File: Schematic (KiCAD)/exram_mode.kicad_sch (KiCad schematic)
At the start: 86 parts

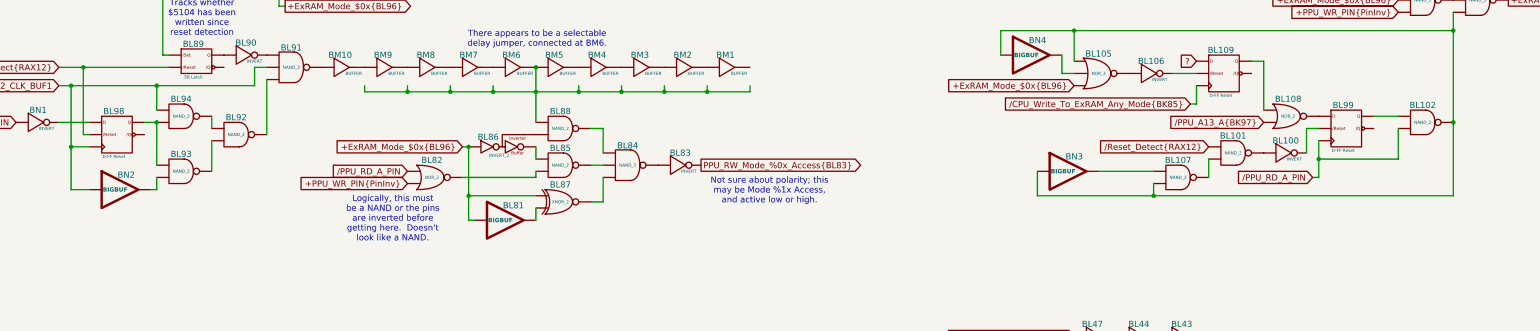
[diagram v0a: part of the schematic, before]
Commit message: - Started work on the pulse channels.  - Solved at least 2 of the red traces in the SVG.  - Finally realized that "Unknown 4to1" cells are actually just ordinary And-Or-Invert "AOI22" cells.
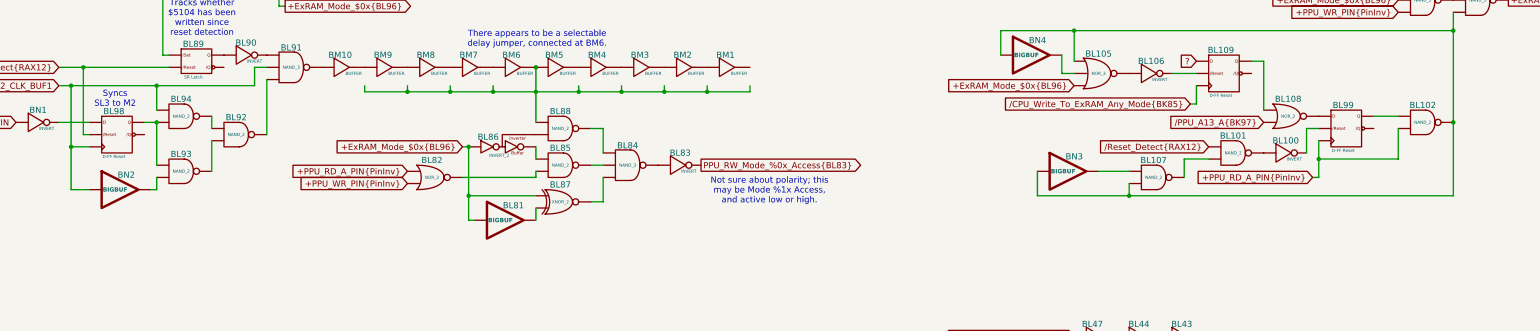
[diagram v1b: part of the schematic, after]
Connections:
- net at BL35. (X): now also BL34. (X), BL37. (X); no longer BL40. (X)
- net at BL31. (X): now also BL32. (X)
- net at BL32. (X): now also BL25. (X), BL28. (X); no longer BL31. (X)
- net at BL45. (X): now also BL41. (X); no longer BL46. (X)
- net at BL29. (X): now also BL35. (X); no longer BL30. (X)
- net +PPU_RD_A_PIN{PinInv}: now reaches BL99. (/Q)
- net +PPU_RD_A_PIN{PinInv}: now also BL102. (X), BL82. (X)
- net at BL100. (X): now also BL101. (X); no longer BL99. (/Q)
- net at BL39. (X): now also BL42. (X)
- net at BL90. (X): now also BL91. (X); no longer BL89. (/Q)
- net at BL44. (X): now also BL43. (X); no longer BL47. (X)
- net at BH9. (X): now also BK43. (X); no longer BH10. (X)
- net at BK43. (X): no longer BH9. (X)
- net at BL93. (X): now also BL92. (X); no longer BN2. (X)
- net at BL41. (X): now also BL42. (X); no longer BL45. (X)
- net at BL88. (X): now also BL86. (X); no longer BL84. (X)
- net at BL92. (X): now also BL94. (X); no longer BL93. (X)
- net at BM9. (X): now also BM10. (X); no longer BM8. (X)
- net at BM10. (X): now also BL91. (X); no longer BM9. (X)
- net at BH1. (X): now also BK41. (X); no longer BH2. (X)
- net at BK41. (X): no longer BH1. (X)
- net at BL84. (X): now also BL85. (X); no longer BL87. (X)
- net at BL85. (X): now also BL86. (X); no longer BL82. (X)
- net at BM3. (X): now also BM4. (X); no longer BM2. (X)
- net at BM4. (X): now also BM5. (X); no longer BM3. (X)
- net at BL106. (X): now also BL109. (/Q); no longer BL105. (X)
- net at BK40. (X): no longer BL9. (X)
- net at BK42. (X): no longer BL8. (X)
- removed net /PPU_RD_A_PIN: BL102. (X), BL82. (X), BL99. (/Q)
- new net: BL35. (X), BL40. (X)
- new net: BL45. (X), BL46. (X)
- new net: BL29. (X), BL32. (X), BL36. (X), BL41. (X), BL43. (X)
- new net: BL29. (X), BL32. (X), BL33. (X)
- new net: BL28. (X), BL29. (X), BL37. (X)
- new net: BL29. (X), BL30. (X)
- new net: BL81. (X), BL87. (X)
- new net: BK84. (X), BL102. (X), BL105. (X), BL107. (X), BN3. (X), BN4. (X)
- new net: BK83. (X), BK84. (X)
- new net: BK84. (X), BK86. (X)
- new net: BL102. (X), BL99. (/Q)
- new net: BL108. (X), BL99. (/Q)
- new net: BL100. (X), BL99. (/Q)
- new net: BL36. (X), BL37. (X)
- new net: BL93. (X), BL94. (X), BL98. (/Q)
- new net: BL98. (/Q), BN1. (X)
- new net: BK79. (X), BK81. (X), BK82. (Q1)
- new net: BL89. (/Q), BL90. (X)
- new net: BL44. (X), BL47. (X)
- new net: BH10. (X), BH9. (X)
- new net: BL93. (X), BN2. (X)
- new net: BK39. (X), BK40. (X), BK42. (X)
- new net: BL37. (X), BL38. (X), BL42. (X)
- new net: BL84. (X), BL88. (X)
- new net: BL88. (X), BM5. (X), BM6. (X)
- new net: BM8. (X), BM9. (X)
- new net: BL108. (X), BL109. (/Q)
- new net: BK79. (X), BK82. (Q1), BL96. (X)
- new net: BH1. (X), BH2. (X)
- new net: BL84. (X), BL87. (X)
- new net: BL82. (X), BL85. (X)
- new net: BL83. (X), BL84. (X)
- new net: BK41. (X), BK43. (X), BK44. (X)
- new net: BM2. (X), BM3. (X)
- new net: BK80. (X), BK82. (Q1)
- new net: BL105. (X), BL106. (X)
- new net: BL91. (X), BL92. (X)
- new net: BK40. (X), BL9. (X)
- new net: BK42. (X), BL8. (X)
- now unconnected: BK40. (X), BK41. (X), BK42. (X), BK43. (X)
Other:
- note added: "Syncs SL3 to M2"
- note removed: "Logically, this must be a NAND or the pins are inverted before getting here. Doesn't look like a NAND."
- moved on the sheet: BL107
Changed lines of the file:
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@@
 		)
 	)
-	(text "There appears to be a selectable\ndelay jumper, connected at BM6."
+	(text "Syncs\nSL3 to M2"
 		(exclude_from_sim no)
-		(at 151.384 103.378 0)
+		(at 63.754 115.824 0)
 		(effects
 			(font
@@
 		)
 	)
-	(text "Logically, this must\nbe a NAND or the pins\nare inverted before\ngetting here.  Doesn't\nlook like a NAND."
+	(text "There appears to be a selectable\ndelay jumper, connected at BM6."
 		(exclude_from_sim no)
-		(at 121.412 140.716 0)
+		(at 151.384 103.378 0)
 		(effects
 			(font
@@
 	)
 	(junction
+		(at 274.32 135.89)
+		(diameter 0)
+		(color 0 0 0 0)
+	)
+	(junction
 		(at 290.83 204.47)
 		(diameter 0)
@@
 	)
 	(junction
-		(at 279.4 135.89)
-		(diameter 0)
-		(color 0 0 0 0)
-	)
-	(junction
 		(at 54.61 113.03)
 		(diameter 0)
@@
 	(wire
 		(pts
-			(xy 267.97 130.81) (xy 279.4 130.81)
+			(xy 267.97 130.81) (xy 274.32 130.81)
 		)
 		(stroke
@@
 	(wire
 		(pts
-			(xy 341.63 135.89) (xy 279.4 135.89)
-		)
-		(stroke
-			(width 0)
-			(type default)
-		)
-	)
-	(wire
-		(pts
 			(xy 177.8 113.03) (xy 177.8 114.3)
 		)
@@
 	(wire
 		(pts
-			(xy 290.83 128.27) (xy 290.83 132.08)
+			(xy 285.75 128.27) (xy 285.75 132.08)
 		)
 		(stroke
@@
 	(wire
 		(pts
+			(xy 274.32 135.89) (xy 255.27 135.89)
+		)
+		(stroke
+			(width 0)
+			(type default)
+		)
+	)
+	(wire
+		(pts
 			(xy 52.07 113.03) (xy 54.61 113.03)
 		)
@@
 	(wire
 		(pts
-			(xy 279.4 135.89) (xy 279.4 133.35)
+			(xy 274.32 135.89) (xy 274.32 133.35)
 		)
 		(stroke
@@
 	(wire
 		(pts
+			(xy 285.75 128.27) (xy 290.83 128.27)
+		)
+		(stroke
+			(width 0)
+			(type default)
+		)
+	)
+	(wire
+		(pts
+			(xy 274.32 135.89) (xy 341.63 135.89)
+		)
+		(stroke
+			(width 0)
+			(type default)
+		)
+	)
+	(wire
+		(pts
 			(xy 328.93 165.1) (xy 290.83 165.1)
 		)
@@
 	(wire
 		(pts
-			(xy 279.4 135.89) (xy 255.27 135.89)
-		)
-		(stroke
-			(width 0)
-			(type default)
-		)
-	)
-	(wire
-		(pts
 			(xy 323.85 74.93) (xy 327.66 74.93)
 		)
@@
 		)
 	)
-	(global_label "{slash}PPU_RD_A_PIN"
+	(global_label "+PPU_RD_A_PIN{PinInv}"
 		(shape input)
 		(at 124.46 130.81 180)
@@
 		)
 		(property "Intersheetrefs" "${INTERSHEET_REFS}"
-			(at 106.5371 130.81 0)
+			(at 98.8566 130.81 0)
 			(effects
 				(font
@@
 		)
 	)
-	(global_label "{slash}PPU_RD_A_PIN"
+	(global_label "+PPU_RD_A_PIN{PinInv}"
 		(shape input)
 		(at 312.42 132.08 180)
@@
 		)
 		(property "Intersheetrefs" "${INTERSHEET_REFS}"
-			(at 294.4971 132.08 0)
+			(at 286.8166 132.08 0)
 			(effects
 				(font
@@
 		(lib_name "NAND_2_11")
 		(lib_id "MMC5:NAND_2")
-		(at 284.48 132.08 0)
+		(at 279.4 132.08 0)
 		(unit 1)
 		(exclude_from_sim no)
@@
 		(fields_autoplaced yes)
 		(property "Reference" "BL107"
-			(at 284.48 127.762 0)
+			(at 279.4 127.762 0)
 			(do_not_autoplace yes)
 			(effects
@@
 		)
 		(property "Value" "NAND_2"
-			(at 284.48 132.08 0)
+			(at 279.4 132.08 0)
 			(do_not_autoplace yes)
 			(effects
@@
 		)
 		(property "Footprint" ""
-			(at 284.48 132.08 0)
+			(at 279.4 132.08 0)
 			(effects
 				(font
@@
 		)
 		(property "Datasheet" ""
-			(at 284.48 132.08 0)
+			(at 279.4 132.08 0)
 			(effects
 				(font
@@
 		)
 		(property "Description" ""
-			(at 284.48 132.08 0)
+			(at 279.4 132.08 0)
 			(effects
 				(font

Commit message: Schematic Updates:  - Added all 10-bit CHR banking registers $5120 - $512B, including where all 10 bits come from when written.  - Added 8-bit CHR bank register $5202, which is the bank used when rendering the V-Split region.    + V-Split seems to always be 8-bit, 8kB bank regardless of CHR mode.  The wiki doesn't say that and I don't know for sure.  - Added decoding logic that activates the correct CHR bank for CHR A10, A11, A12 (corresponding to columns AV, AW, AX).  - Noted, AX15 activates $5202 CHR Bank for V-Split region.  AX16 activates CHR Bank from data stored in ExRAM for extended attributes.  Therefore, AX15 driven by AT1 High means we specifically are in v-split region, and not extended attribute mode.  With this knowledge, backtracking up the chain from AT1 to N14 sheds very useful insight what the 3-bit shift register at N11/N12/N13 is doing.  We now know that N14 goes low specifically for pattern table fetches when rendering the V-split region, and does not appear dual-purposed for extended attribute fetch sequencing.  This may seem rather subtle or unimportant, but it is a good advancement for higher level understanding what that mysterious shift register might be doing.
SVG Trace Updates:
 - Registers $5120, 5121, 5122, 5123 (first 4 CHR bank register), the outputs were labeled in reverse order.
 - Register $5130 (highest CHR bank bits), the outputs were labeled with backwards polarity.  The error was not having taken into account that the CPU data bus input to the latches came already inverted to begin with.
 - Still wrong: Cell AV7, 2-input NAND gate.  One of the inputs is missing and it logically should be driven by AS19 like the 4 cells to its direct right.  I can't quite make out how it makes that connection.
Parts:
- removed BH1, BH10, BH2, BH9, BL28, BL30, BL31, BL38, BL39, BL40, BL43, BL44, BL45: INVERT, symbol MMC5:INVERT
- removed BH11, BH3: NAND_5, symbol MMC5:NAND_5
- removed BK39, BK44, BL10, BL11, BL33, BL34, BL46, BL47, BL8, BL9: BUFFER, symbol MMC5:BUFFER
- removed BK40, BK41, BK42, BK43, BL35, BL36, BL41: NAND_2, symbol MMC5:NAND_2
- removed BL25, BL29: NAND_4, symbol MMC5:NAND_4
- removed BL32, BL37, BL42: NAND_3, symbol MMC5:NAND_3
- added BJ10, BJ12(a), BJ12(b), BJ12(c), BJ12(d), BJ12(e), BJ12(f), BJ12(g), BJ12(h): BUFFER, symbol MMC5:BUFFER
- added BJ11: Reg 8 D-Latch N, symbol MMC5:Reg_8_D-Latch_N
- added BJ7: INVERT, symbol MMC5:INVERT
- added BJ9: NAND_3, symbol MMC5:NAND_3
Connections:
- net at BL100. (X): now also BL101. (X); no longer BL99. (/Q)
- net at BL90. (X): now also BL91. (X); no longer BL89. (/Q)
- net at BL93. (X): now also BL92. (X); no longer BN2. (X)
- net at BL88. (X): now also BL86. (X); no longer BL84. (X)
- net at BL92. (X): now also BL94. (X); no longer BL93. (X)
- net at BM9. (X): now also BM10. (X); no longer BM8. (X)
- net at BM10. (X): now also BL91. (X); no longer BM9. (X)
- net at BL84. (X): now also BL85. (X); no longer BL87. (X)
- net at BL85. (X): now also BL86. (X); no longer BL82. (X)
- net at BM3. (X): now also BM4. (X); no longer BM2. (X)
- net at BM4. (X): now also BM5. (X); no longer BM3. (X)
- net at BL106. (X): now also BL109. (/Q); no longer BL105. (X)
- new net: BL81. (X), BL87. (X)
- new net: BK84. (X), BL102. (X), BL105. (X), BL107. (X), BN3. (X), BN4. (X)
- new net: BK83. (X), BK84. (X)
- new net: BK84. (X), BK86. (X)
- new net: BL102. (X), BL99. (/Q)
- new net: BL108. (X), BL99. (/Q)
- new net: BL100. (X), BL99. (/Q)
- new net: BL93. (X), BL94. (X), BL98. (/Q)
- new net: BL98. (/Q), BN1. (X)
- new net: BK79. (X), BK81. (X), BK82. (Q1)
- new net: BL89. (/Q), BL90. (X)
- new net: BL93. (X), BN2. (X)
- new net: BJ7. (X), BJ9. (X)
- new net: BJ10. (X), BJ9. (X)
- new net: BL84. (X), BL88. (X)
- new net: BL88. (X), BM5. (X), BM6. (X)
- new net: BM8. (X), BM9. (X)
- new net: BL108. (X), BL109. (/Q)
- new net: BK79. (X), BK82. (Q1), BL96. (X)
- new net: BJ10. (X), BJ11. (/Q7)
- new net: BL84. (X), BL87. (X)
- new net: BL82. (X), BL85. (X)
- new net: BL83. (X), BL84. (X)
- new net: BM2. (X), BM3. (X)
- new net: BK80. (X), BK82. (Q1)
- new net: BL105. (X), BL106. (X)
- new net: BL91. (X), BL92. (X)
- new net +ExRAM_Read_D6_Latch{BJ11}: BJ11. (/Q7)
- new net +ExRAM_Read_D7_Latch{BJ11}: BJ11. (/Q7)
- new net +PPU_Fetch_Count.0{S10}: BJ7. (X)
- new net +PPU_Fetch_Count.1{S13}: BJ9. (X)
- new net +PPU_RD_A{BJ8}: BJ9. (X)
- new net ExRAM_D0_Read: BJ12(a). (X)
- new net ExRAM_D0_Read{BJ12(a)}: BJ11. (/Q7), BJ12(a). (X)
- new net ExRAM_D1_Read: BJ12(b). (X)
- new net ExRAM_D1_Read{BJ12(b)}: BJ11. (/Q7), BJ12(b). (X)
- new net ExRAM_D2_Read: BJ12(c). (X)
- new net ExRAM_D2_Read{BJ12(c)}: BJ11. (/Q7), BJ12(c). (X)
- new net ExRAM_D3_Read: BJ12(d). (X)
- new net ExRAM_D3_Read{BJ12(d)}: BJ11. (/Q7), BJ12(d). (X)
- new net ExRAM_D4_Read: BJ12(e). (X)
- new net ExRAM_D4_Read{BJ12(e)}: BJ11. (/Q7), BJ12(e). (X)
- new net ExRAM_D5_Read: BJ12(f). (X)
- new net ExRAM_D5_Read{BJ12(f)}: BJ11. (/Q7), BJ12(f). (X)
- new net ExRAM_D6_Read: BJ12(g). (X)
- new net ExRAM_D6_Read{BJ12(g)}: BJ11. (/Q7), BJ12(g). (X)
- new net ExRAM_D7_Read: BJ12(h). (X)
- new net ExRAM_D7_Read{BJ12(h)}: BJ11. (/Q7), BJ12(h). (X)
- new net /ExRAM_Read_D0_Latch{BJ11}: BJ11. (/Q7)
- new net /ExRAM_Read_D1_Latch{BJ11}: BJ11. (/Q7)
- new net /ExRAM_Read_D2_Latch{BJ11}: BJ11. (/Q7)
- new net /ExRAM_Read_D3_Latch{BJ11}: BJ11. (/Q7)
- new net /ExRAM_Read_D4_Latch{BJ11}: BJ11. (/Q7)
- new net /ExRAM_Read_D5_Latch{BJ11}: BJ11. (/Q7)
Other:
- note removed: "/Extended Attributes Enabled"
- moved on the sheet: BK79, BK80, BK81, BK82, BK83, BK84, BK85, BK86, BK87, BL100, BL101, BL102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
